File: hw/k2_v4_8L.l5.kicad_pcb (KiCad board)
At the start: 8 copper layers, 120 x 46 mm, 59 parts, among them J11 J_EC_HEADER, J12 J_12V_IN, J13 J_SWD, J2 SlimSAS_x8_SFF8654, J3 MCIO_4i_SFF1016, J4 MCIO_4i_SFF1016, J6 J_PWR_CTRL, J9 J_OOB_HEADER, U1 STM32G0B1CBT6, U2 DCDC_12V_3V3, U4 BAT54C, U5 OPTO_LTV356T, U6 DS320PR1601

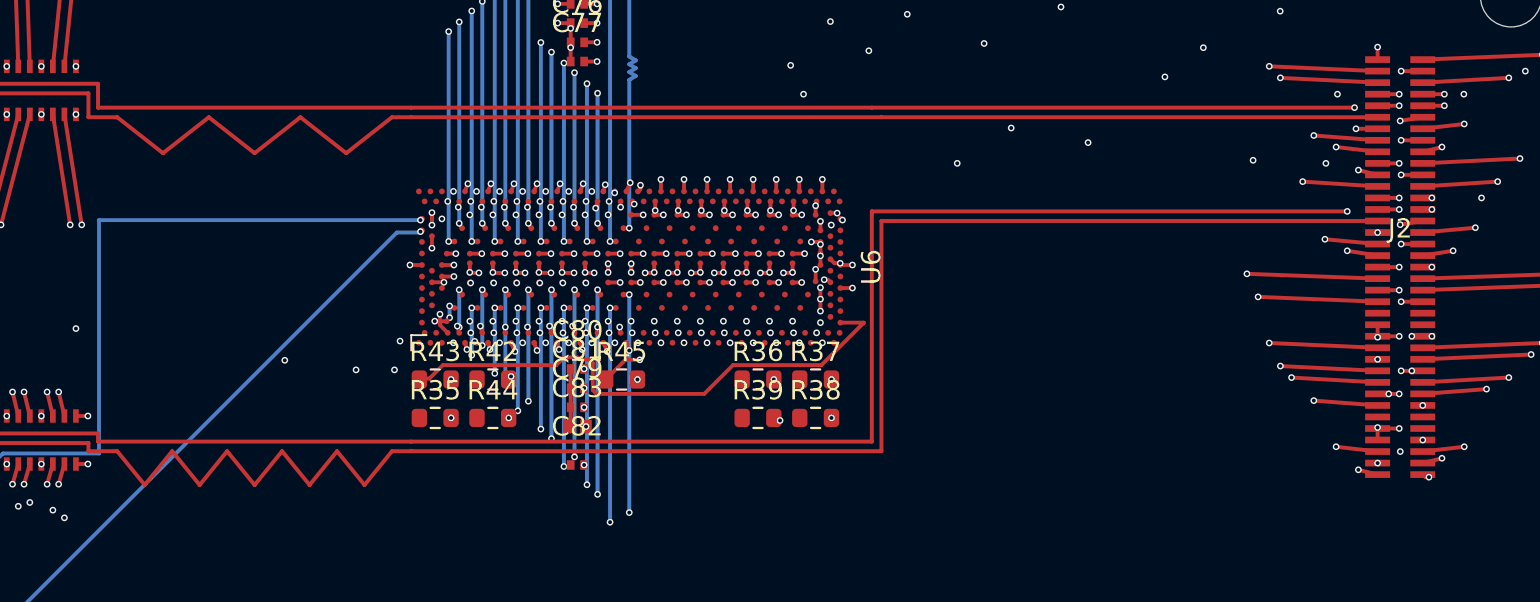
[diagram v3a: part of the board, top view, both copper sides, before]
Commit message: p4(k2): 增量 10（L2 自裁，U4-D/G-1 试点）—— REFCLK 两对设计层重派生 0/45/90 + 对内等长修复（非45 2051→2032，对内 max 1.1046→0.0787，违规/连通不退化）+ T-13/T-14 登记
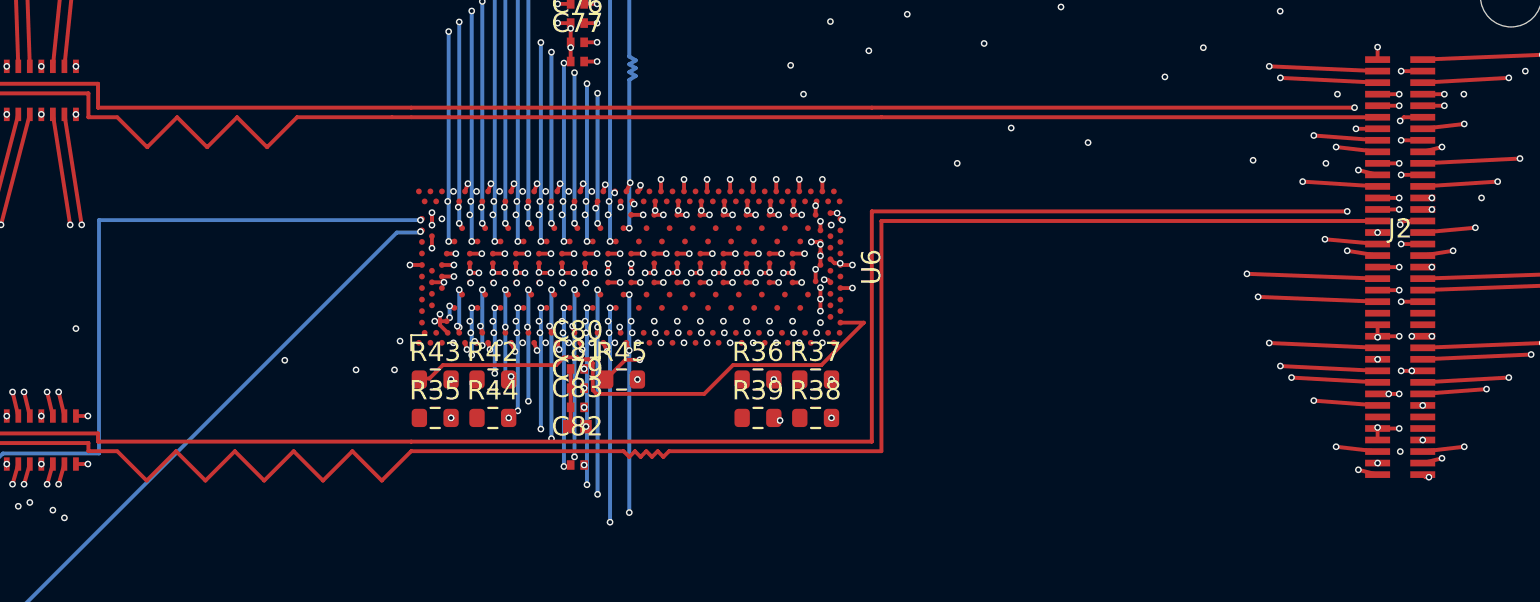
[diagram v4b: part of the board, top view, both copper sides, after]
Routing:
- net PCIE_REFCLK1_P: track 94.7 -> 93.7 mm
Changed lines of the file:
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@@
 	)
 	(segment
-		(start 71.816668 45.9)
-		(end 69.433335 47.769878)
-		(width 0.205)
+		(start 67.05 45.9)
+		(end 68.6095 47.4595)
+		(width 0.2)
+		(layer "F.Cu")
+		(net "PCIE_REFCLK0_P")
+	)
+	(segment
+		(start 73.288 45.9)
+		(end 74.8475 47.4595)
+		(width 0.2)
 		(layer "F.Cu")
 		(net "PCIE_REFCLK0_P")
@@
 	)
 	(segment
+		(start 68.6095 47.4595)
+		(end 70.169 45.9)
+		(width 0.2)
+		(layer "F.Cu")
+		(net "PCIE_REFCLK0_P")
+	)
+	(segment
 		(start 81.35 45.9)
-		(end 78.966667 47.769878)
-		(width 0.205)
-		(layer "F.Cu")
-		(net "PCIE_REFCLK0_P")
-	)
-	(segment
-		(start 82.35 45.9)
-		(end 81.35 45.9)
-		(width 0.205)
-		(layer "F.Cu")
-		(net "PCIE_REFCLK0_P")
-	)
-	(segment
-		(start 74.200001 47.769878)
-		(end 71.816668 45.9)
-		(width 0.205)
-		(layer "F.Cu")
-		(net "PCIE_REFCLK0_P")
-	)
-	(segment
-		(start 76.583334 45.9)
-		(end 74.200001 47.769878)
-		(width 0.205)
-		(layer "F.Cu")
-		(net "PCIE_REFCLK0_P")
-	)
-	(segment
-		(start 78.966667 47.769878)
-		(end 76.583334 45.9)
-		(width 0.205)
+		(end 82.35 45.9)
+		(width 0.2)
 		(layer "F.Cu")
 		(net "PCIE_REFCLK0_P")
@@
 	)
 	(segment
-		(start 69.433335 47.769878)
-		(end 67.050002 45.9)
-		(width 0.205)
+		(start 71.7285 47.4595)
+		(end 73.288 45.9)
+		(width 0.2)
+		(layer "F.Cu")
+		(net "PCIE_REFCLK0_P")
+	)
+	(segment
+		(start 74.8475 47.4595)
+		(end 76.407 45.9)
+		(width 0.2)
+		(layer "F.Cu")
+		(net "PCIE_REFCLK0_P")
+	)
+	(segment
+		(start 76.407 45.9)
+		(end 81.35 45.9)
+		(width 0.2)
 		(layer "F.Cu")
 		(net "PCIE_REFCLK0_P")
@@
 	)
 	(segment
+		(start 70.169 45.9)
+		(end 71.7285 47.4595)
+		(width 0.2)
+		(layer "F.Cu")
+		(net "PCIE_REFCLK0_P")
+	)
+	(segment
+		(start 135 45.9)
+		(end 134.015 45.9)
+		(width 0.2)
+		(layer "F.Cu")
+		(net "PCIE_REFCLK0_N")
+	)
+	(segment
 		(start 66.05 44.1575)
 		(end 58.3 44.1575)
@@
 	)
 	(segment
-		(start 135 45.9)
-		(end 133.824999 46.09)
-		(width 0.205)
+		(start 134.015 45.9)
+		(end 133.825 46.09)
+		(width 0.2)
 		(layer "F.Cu")
 		(net "PCIE_REFCLK0_N")
@@
 	)
 	(segment
-		(start 133.824999 46.09)
-		(end 131.449999 45.4)
-		(width 0.16)
+		(start 133.825 46.09)
+		(end 133.135 45.4)
+		(width 0.2)
 		(layer "In2.Cu")
 		(net "PCIE_REFCLK0_N")
 	)
 	(segment
+		(start 133.135 45.4)
+		(end 131.45 45.4)
+		(width 0.2)
+		(layer "In2.Cu")
+		(net "PCIE_REFCLK0_N")
+	)
+	(segment
+		(start 67.05 63.282)
+		(end 68.58 64.812)
+		(width 0.2)
+		(layer "F.Cu")
+		(net "PCIE_REFCLK1_P")
+	)
+	(segment
+		(start 74.7 64.812)
+		(end 76.23 63.282)
+		(width 0.2)
+		(layer "F.Cu")
+		(net "PCIE_REFCLK1_P")
+	)
+	(segment
 		(start 82.35 63.282)
-		(end 81.35 63.282)
-		(width 0.205)
-		(layer "F.Cu")
-		(net "PCIE_REFCLK1_P")
-	)
-	(segment
-		(start 71.34 65.039783)
-		(end 69.91 63.282)
-		(width 0.205)
+		(end 93.4031 63.282)
+		(width 0.2)
+		(layer "F.Cu")
+		(net "PCIE_REFCLK1_P")
+	)
+	(segment
+		(start 95.1797 63.282)
+		(end 95.4758 63.5781)
+		(width 0.2)
+		(layer "F.Cu")
+		(net "PCIE_REFCLK1_P")
+	)
+	(segment
+		(start 73.17 63.282)
+		(end 74.7 64.812)
+		(width 0.2)
+		(layer "F.Cu")
+		(net "PCIE_REFCLK1_P")
+	)
+	(segment
+		(start 77.76 64.812)
+		(end 79.29 63.282)
+		(width 0.2)
+		(layer "F.Cu")
+		(net "PCIE_REFCLK1_P")
+	)
+	(segment
+		(start 70.11 63.282)
+		(end 71.64 64.812)
+		(width 0.2)
+		(layer "F.Cu")
+		(net "PCIE_REFCLK1_P")
+	)
+	(segment
+		(start 94.8836 63.5781)
+		(end 95.1797 63.282)
+		(width 0.2)
 		(layer "F.Cu")
 		(net "PCIE_REFCLK1_P")
@@
 	)
 	(segment
+		(start 95.7719 63.282)
+		(end 106.825 63.282)
+		(width 0.2)
+		(layer "F.Cu")
+		(net "PCIE_REFCLK1_P")
+	)
+	(segment
 		(start 106.825 51.3)
 		(end 106.825 63.282)
@@
 	)
 	(segment
-		(start 74.2 65.039783)
-		(end 72.77 63.282)
-		(width 0.205)
-		(layer "F.Cu")
-		(net "PCIE_REFCLK1_P")
-	)
-	(segment
-		(start 68.48 65.039783)
-		(end 67.05 63.282)
-		(width 0.205)
-		(layer "F.Cu")
-		(net "PCIE_REFCLK1_P")
-	)
-	(segment
-		(start 75.63 63.282)
-		(end 74.2 65.039783)
-		(width 0.205)
+		(start 93.6992 63.5781)
+		(end 93.9953 63.282)
+		(width 0.2)
+		(layer "F.Cu")
+		(net "PCIE_REFCLK1_P")
+	)
+	(segment
+		(start 71.64 64.812)
+		(end 73.17 63.282)
+		(width 0.2)
+		(layer "F.Cu")
+		(net "PCIE_REFCLK1_P")
+	)
+	(segment
+		(start 68.58 64.812)
+		(end 70.11 63.282)
+		(width 0.2)
+		(layer "F.Cu")
+		(net "PCIE_REFCLK1_P")
+	)
+	(segment
+		(start 93.9953 63.282)
+		(end 94.2914 63.5781)
+		(width 0.2)
 		(layer "F.Cu")
 		(net "PCIE_REFCLK1_P")
@@
 	)
 	(segment
+		(start 76.23 63.282)
+		(end 77.76 64.812)
+		(width 0.2)
+		(layer "F.Cu")
+		(net "PCIE_REFCLK1_P")
+	)
+	(segment
 		(start 67.05 63.282)
 		(end 65.55 63.282)
@@
 	)
 	(segment
-		(start 106.825 63.282)
+		(start 93.4031 63.282)
+		(end 93.6992 63.5781)
+		(width 0.2)
+		(layer "F.Cu")
+		(net "PCIE_REFCLK1_P")
+	)
+	(segment
+		(start 79.29 63.282)
+		(end 80.82 64.812)
+		(width 0.2)
+		(layer "F.Cu")
+		(net "PCIE_REFCLK1_P")
+	)
+	(segment
+		(start 80.82 64.812)
 		(end 82.35 63.282)
-		(width 0.205)
-		(layer "F.Cu")
-		(net "PCIE_REFCLK1_P")
-	)
-	(segment
-		(start 69.91 63.282)
-		(end 68.48 65.039783)
-		(width 0.205)
-		(layer "F.Cu")
-		(net "PCIE_REFCLK1_P")
-	)
-	(segment
-		(start 77.06 65.039783)
-		(end 75.63 63.282)
-		(width 0.205)
+		(width 0.2)
 		(layer "F.Cu")
 		(net "PCIE_REFCLK1_P")
@@
 	)
 	(segment
-		(start 72.77 63.282)
-		(end 71.34 65.039783)
-		(width 0.205)
-		(layer "F.Cu")
-		(net "PCIE_REFCLK1_P")
-	)
-	(segment
-		(start 79.92 65.039783)
-		(end 78.49 63.282)
-		(width 0.205)
-		(layer "F.Cu")
-		(net "PCIE_REFCLK1_P")
-	)
-	(segment
-		(start 81.35 63.282)
-		(end 79.92 65.039783)
-		(width 0.205)
-		(layer "F.Cu")
-		(net "PCIE_REFCLK1_P")
-	)
-	(segment
-		(start 78.49 63.282)
-		(end 77.06 65.039783)
-		(width 0.205)
-		(layer "F.Cu")
-		(net "PCIE_REFCLK1_P")
+		(start 94.5875 63.282)
+		(end 94.8836 63.5781)
+		(width 0.2)
+		(layer "F.Cu")
+		(net "PCIE_REFCLK1_P")
+	)
+	(segment
+		(start 94.2914 63.5781)
+		(end 94.5875 63.282)
+		(width 0.2)
+		(layer "F.Cu")
+		(net "PCIE_REFCLK1_P")
+	)
+	(segment
+		(start 95.4758 63.5781)
+		(end 95.7719 63.282)
+		(width 0.2)
+		(layer "F.Cu")
+		(net "PCIE_REFCLK1_P")
+	)
+	(segment
+		(start 134.015 51.3)
+		(end 133.825 51.49)
+		(width 0.2)
+		(layer "F.Cu")
+		(net "PCIE_REFCLK1_N")
 	)
 	(segment
@@
 	)
 	(segment
+		(start 135 51.3)
+		(end 134.015 51.3)
+		(width 0.2)
+		(layer "F.Cu")
+		(net "PCIE_REFCLK1_N")
+	)
+	(segment
 		(start 106.325 50.8)
 		(end 106.325 62.782)
@@
 		(width 0.205)
 		(layer "F.Cu")
-		(net "PCIE_REFCLK1_N")
-	)
-	(segment
-		(start 135 51.3)
-		(end 133.824999 51.49)
-		(width 0.205)
-		(layer "F.Cu")

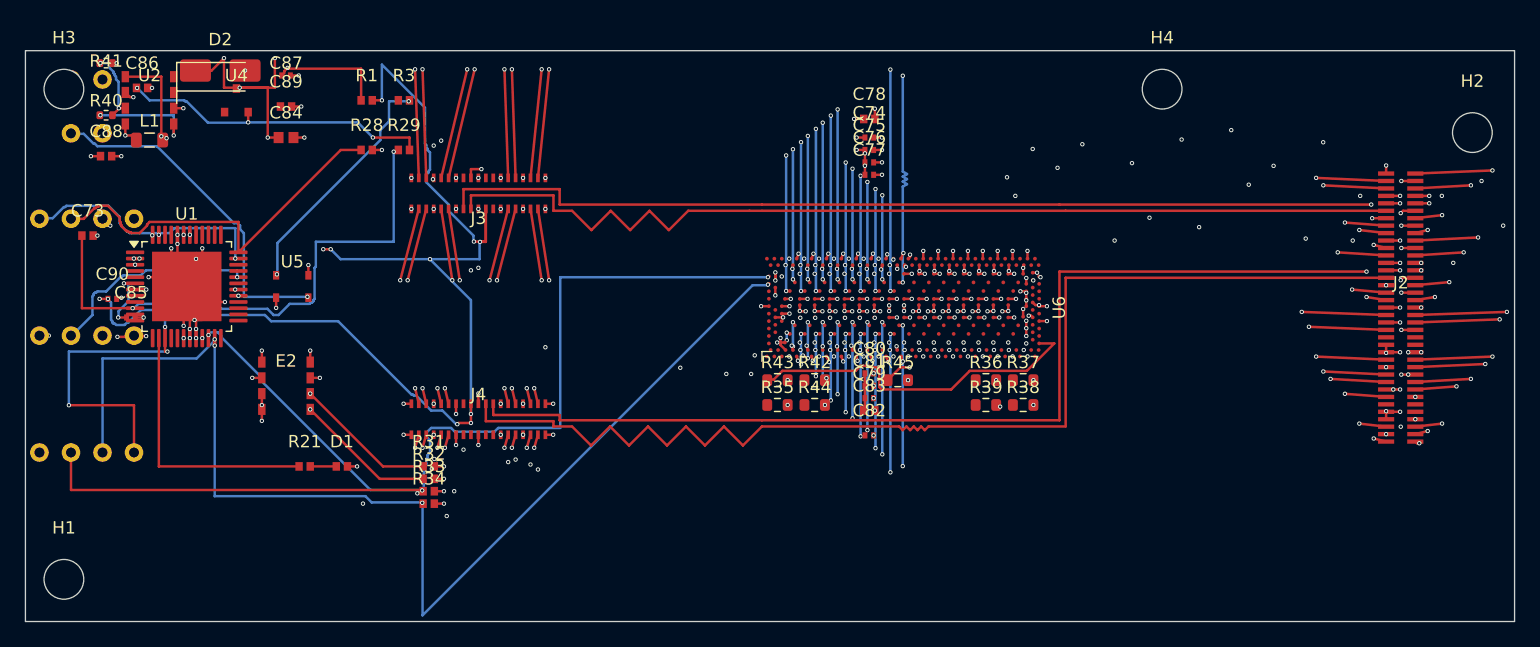
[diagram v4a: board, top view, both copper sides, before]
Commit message: p4(k2): 增量 11（L2 自裁，U4-D/G-1 规模化）—— 全板非45 2032→0 设计层重派生（蛇形梳齿 + 扇出贴合阶梯），违规 75→70、未连接 19→19 不退化、判定 non45 PASS + T-15..T-18 登记
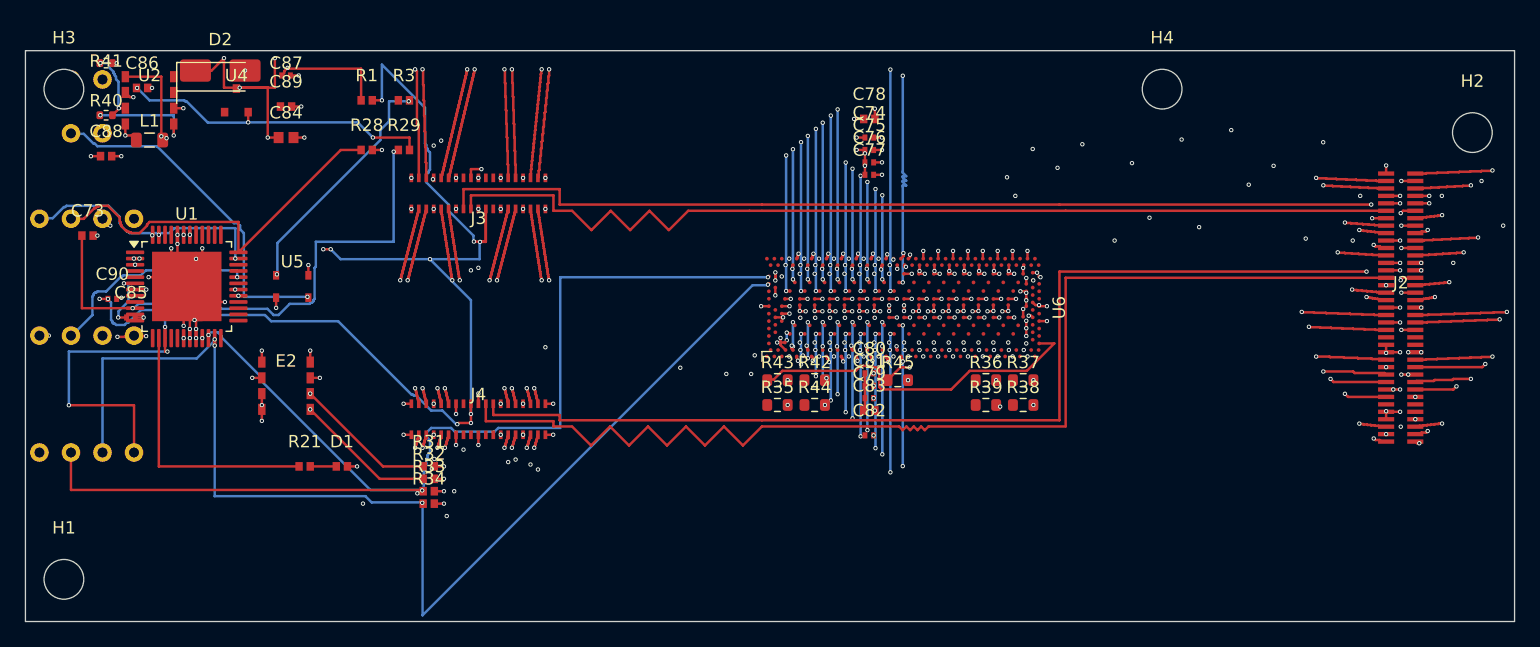
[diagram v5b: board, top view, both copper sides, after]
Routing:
- net PCIE_UP2_N: track 53.4 -> 54.0 mm
- net PCIE_UP2_P: track 53.4 -> 54.0 mm

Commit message: p4(k2): 增量 12（L2 自裁，电源面接入）—— U6 P3V3 二球落 F→In4 盘中孔，未连接 19→17、违规 70→70 零新增 + T-19..T-22 登记
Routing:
- net P3V3: vias 41 -> 43
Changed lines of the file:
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@@
+		(net "P3V3")
+	)
+	(via blind
+		(at 104.17 55.69)
+		(size 0.35)
+		(drill 0.2)
+		(layers "F.Cu" "In4.Cu")
+		(net "P3V3")
+	)
+	(via blind
+		(at 104.69 55.99)
+		(size 0.35)
+		(drill 0.2)
+		(layers "F.Cu" "In4.Cu")
 		(net "P3V3")
 	)

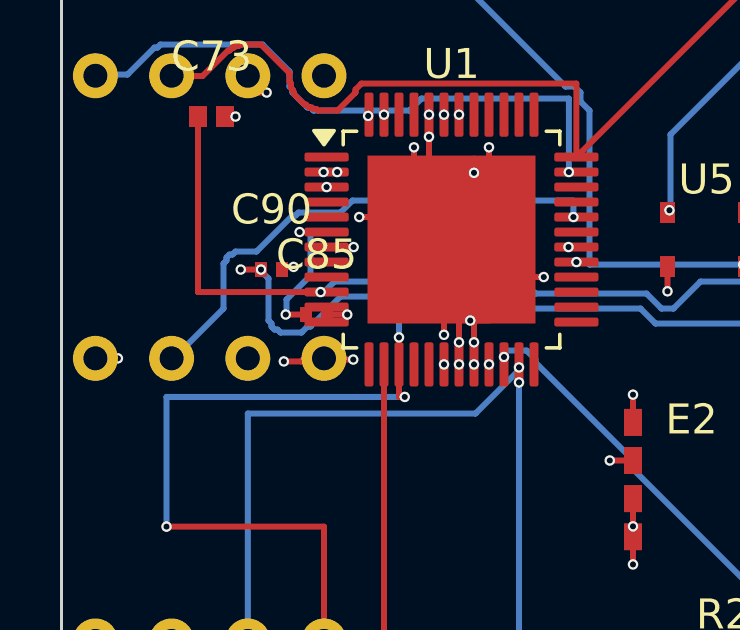
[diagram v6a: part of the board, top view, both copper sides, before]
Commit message: p4(k2): 增量 13（L2 自裁，U1/C85 邻域）—— 定性=放置缺陷：C85 搬 (31.5,54.5,0)->(29.7,54.5,180) + GND 孔改 F->In1 盘中孔，违规 70->51、未连接 17->17 集合同一 + T-24/T-25 登记
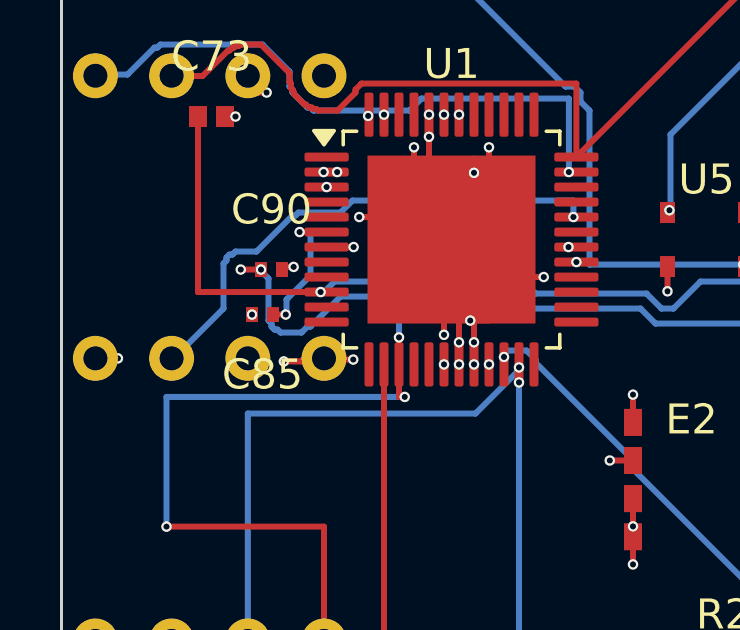
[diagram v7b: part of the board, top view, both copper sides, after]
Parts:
- moved C85 1.80 mm to (29.7, 54.5), turned to 180 degrees
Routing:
- net GND: track 95.7 -> 95.0 mm
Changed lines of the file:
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@@
 	(footprint "Capacitor_SMD:C_0402_1005Metric"
 		(layer "F.Cu")
-		(at 31.5 54.5)
+		(at 29.7 54.5 180)
 		(property "Reference" "C85"
 			(at 0 -2 0)
@@
 	)
 	(segment
-		(start 31.85 54.5)
-		(end 32.525 54.5)
-		(width 0.2)
-		(layer "F.Cu")
-		(net "GND")
-	)
-	(segment
 		(start 36.25 54.7)
 		(end 36.25 55.425)
@@
 	)
 	(via blind
+		(at 29.35 54.5)
+		(size 0.35)
+		(drill 0.2)
+		(layers "F.Cu" "In1.Cu")
+		(net "GND")
+	)
+	(via blind
 		(at 91.35 60)
 		(size 0.35)
@@
 	)
 	(via
-		(at 32.525 54.5)
-		(size 0.35)
-		(drill 0.2)
-		(layers "F.Cu" "B.Cu")
-		(net "GND")
-	)
-	(via
 		(at 133.775 45.3)
 		(size 0.35)
@@
 	)
 	(segment
-		(start 31.15 54.5)
+		(start 30.05 54.5)
 		(end 30.475 54.5)
 		(width 0.2)

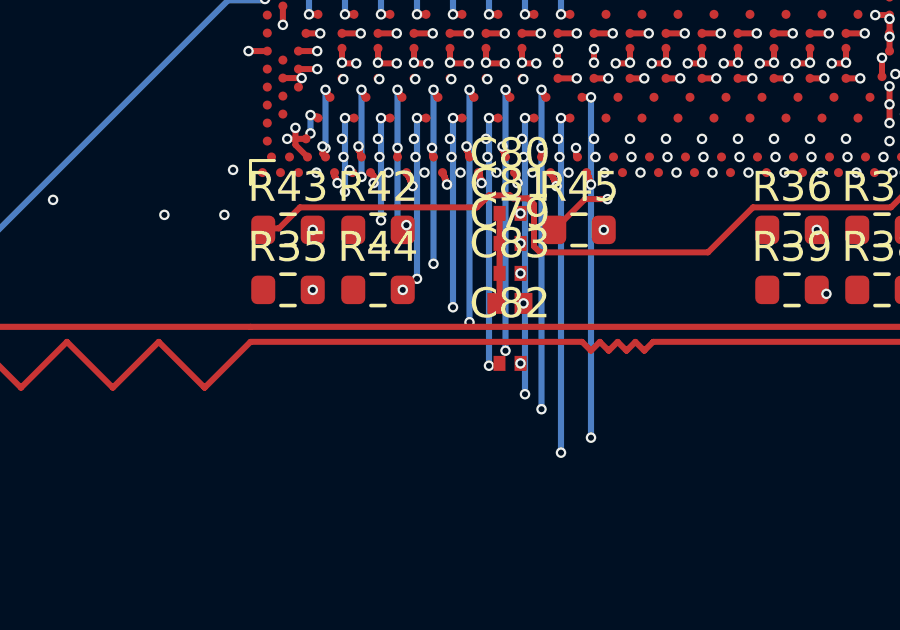
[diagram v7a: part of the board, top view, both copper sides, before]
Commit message: p4(k2): 增量 14（L2 自裁，PDN/走廊/过孔）—— P3V3 去耦列 C79/C80/C81/C83 + C82.1 经 F.Cu 长逃逸接 In4：未连接 17->15、违规 51->51 零新增、复跑逐字节同 + T-27/T-28 登记
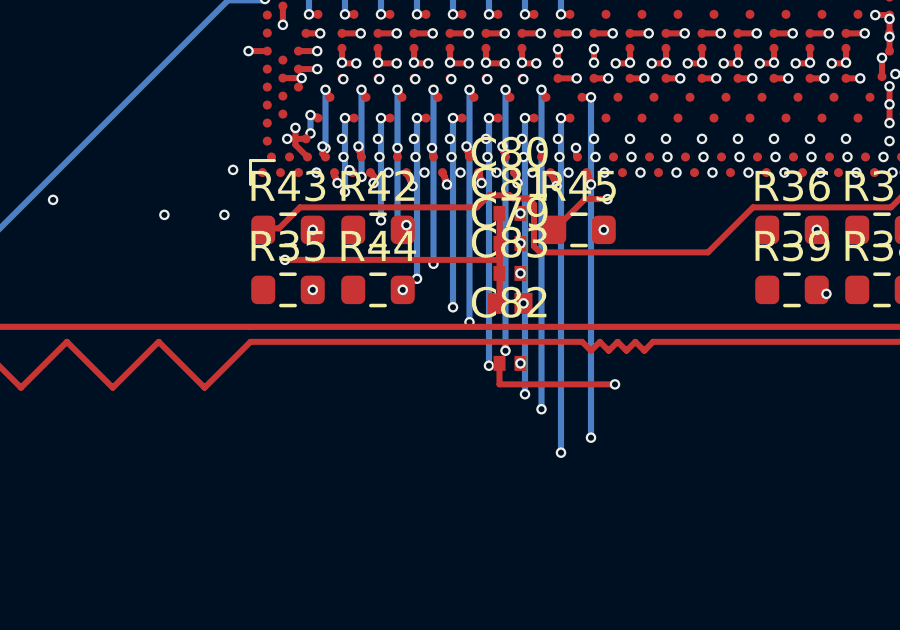
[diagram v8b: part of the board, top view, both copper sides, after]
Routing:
- net P3V3: track 48.7 -> 61.0 mm, vias 43 -> 45
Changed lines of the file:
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@@
 	)
 	(via blind
-		(at 29.35 54.5)
-		(size 0.35)
-		(drill 0.2)
-		(layers "F.Cu" "In1.Cu")
-		(net "GND")
-	)
-	(via blind
 		(at 91.35 60)
 		(size 0.35)
@@
 	)
 	(via blind
+		(at 29.35 54.5)
+		(size 0.35)
+		(drill 0.2)
+		(layers "F.Cu" "In1.Cu")
+		(net "GND")
+	)
+	(via blind
 		(at 35.25 47.8375)
 		(size 0.35)
@@
 	)
 	(segment
+		(start 90.65 60)
+		(end 90.65 60.55)
+		(width 0.2)
+		(layer "F.Cu")
+		(net "P3V3")
+	)
+	(segment
 		(start 87.8 53.5)
 		(end 87.8 53.975)
@@
 	)
 	(segment
+		(start 90.65 60.55)
+		(end 83.5 60.55)
+		(width 0.2)
+		(layer "F.Cu")
+		(net "P3V3")
+	)
+	(segment
 		(start 38 34.6)
 		(end 36.7 34.6)
@@
 	)
 	(segment
+		(start 90.65 64.7)
+		(end 94.5 64.7)
+		(width 0.2)
+		(layer "F.Cu")
+		(net "P3V3")
+	)
+	(segment
 		(start 34.95 38.905)
 		(end 34.95 39.83)
@@
 		(net "P3V3")
 	)
+	(segment
+		(start 90.65 64)
+		(end 90.65 64.7)
+		(width 0.2)
+		(layer "F.Cu")
+		(net "P3V3")
+	)
 	(via
 		(at 102.2 53.975)
@@
 		(net "P3V3")
 	)
+	(via blind
+		(at 83.5 60.55)
+		(size 0.35)
+		(drill 0.2)
+		(layers "F.Cu" "In4.Cu")
+		(net "P3V3")
+	)
 	(via
 		(at 91.875 54)
@@
 		(net "P3V3")
 	)
+	(via blind
+		(at 94.5 64.7)
+		(size 0.35)
+		(drill 0.2)
+		(layers "F.Cu" "In4.Cu")
+		(net "P3V3")
+	)
